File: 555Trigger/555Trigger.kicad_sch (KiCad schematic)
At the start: 23 parts, among them U7 74LVC2G74, U8 74AHC2G00, U9 OPA2333xxD

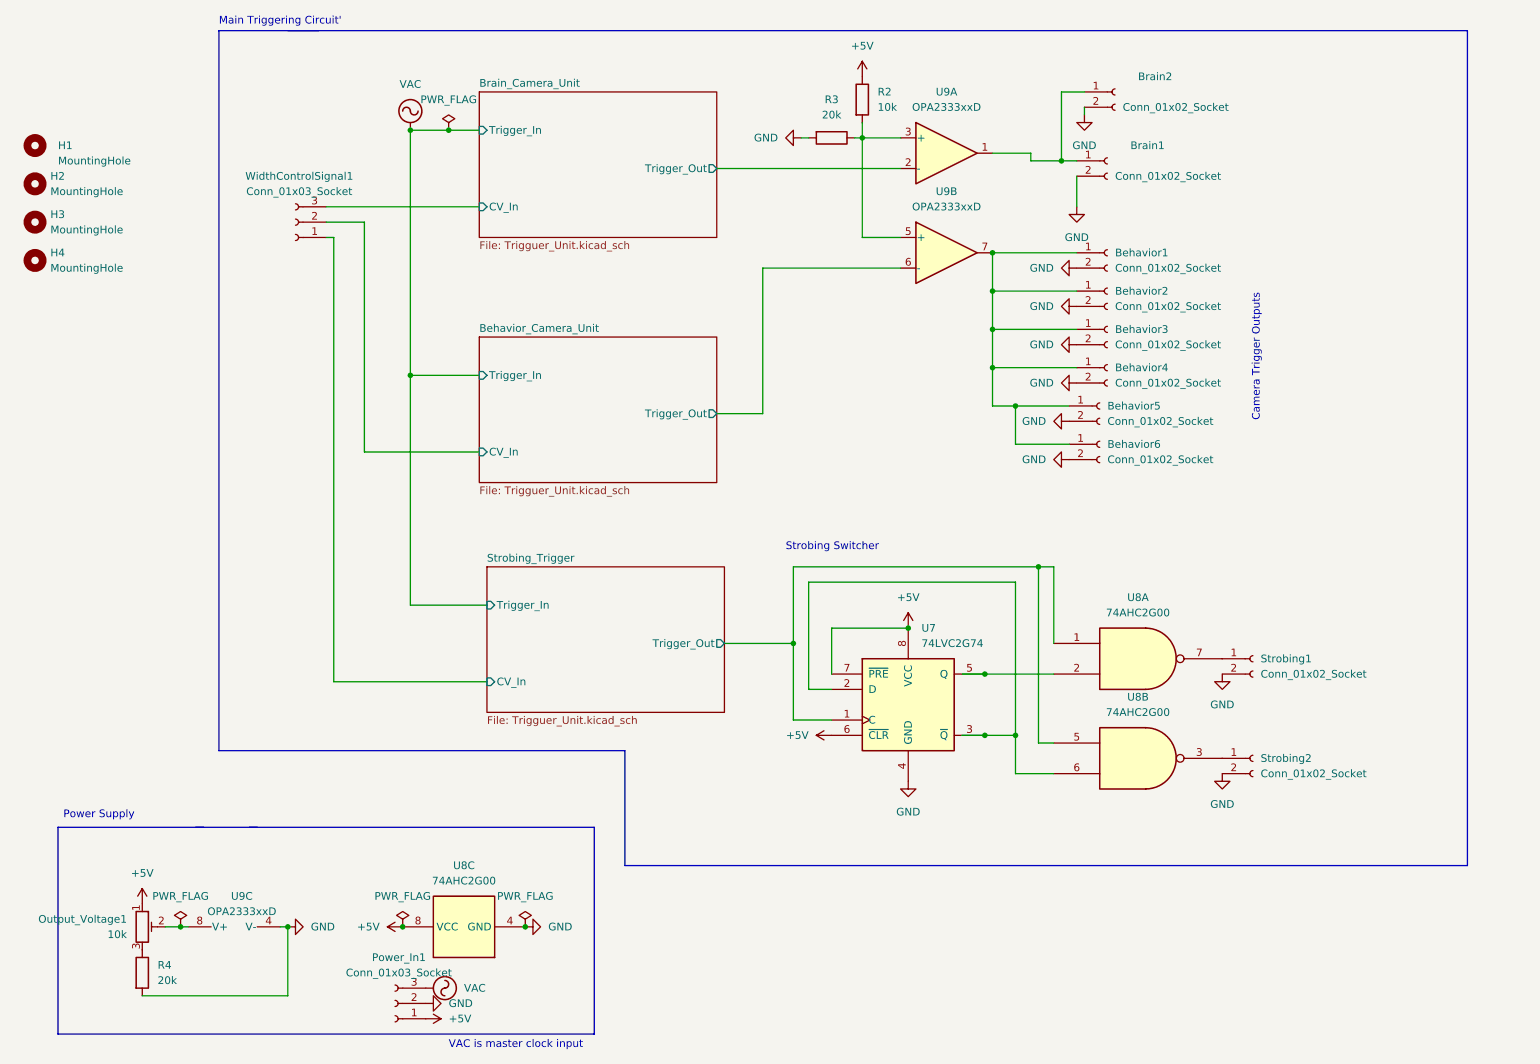
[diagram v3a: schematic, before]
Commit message: changed some components to make manufacturing simpler
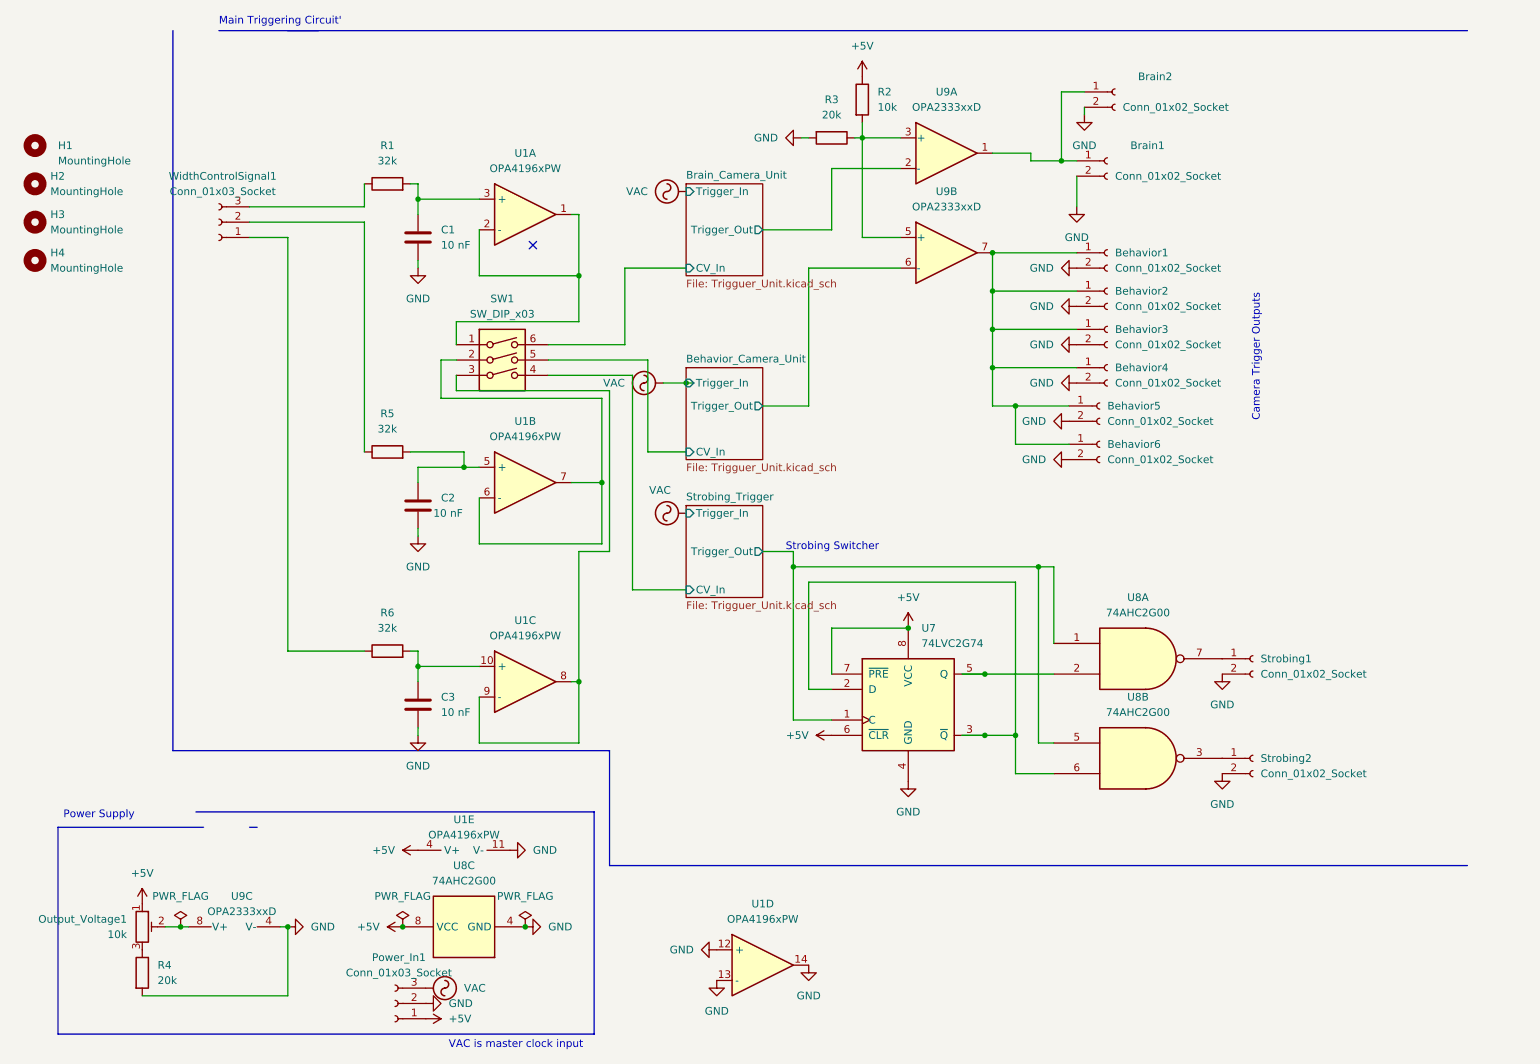
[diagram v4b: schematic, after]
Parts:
- added C1, C2, C3: 10 nF, Capacitor_SMD:C_0603_1608Metric_Pad1.08x0.95mm_HandSolder, symbol Device:C
- added R1, R5, R6: 32k, Resistor_SMD:R_0805_2012Metric_Pad1.20x1.40mm_HandSolder, symbol Device:R
- added SW1: SW_DIP_x03, Button_Switch_SMD:SW_DIP_SPSTx03_Slide_9.78x9.8mm_W8.61mm_P2.54mm, symbol Switch:SW_DIP_x03
- added U1: OPA4196xPW, Package_SO:TSSOP-14_4.4x5mm_P0.65mm, symbol Amplifier_Operational:OPA4196xPW
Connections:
- net +5V: now also U1.4 (V+)
- net Behavior_Camera_Unit/CV_In: now also SW1.5; no longer WidthControlSignal1.2 (Pin_2)
- net Brain_Camera_Unit/CV_In: now also SW1.6; no longer WidthControlSignal1.3 (Pin_3)
- net GND: now also C1.2, C2.2, C3.2, U1.11 (V-), U1.12 (+), U1.13 (-), U1.14
- net Strobing_Trigger/CV_In: now also SW1.4; no longer WidthControlSignal1.1 (Pin_1)
- new net: R6.1, WidthControlSignal1.1 (Pin_1)
- new net: R5.1, WidthControlSignal1.2 (Pin_2)
- new net: R1.1, WidthControlSignal1.3 (Pin_3)
- new net: C1.1, R1.2, U1.3 (+)
- new net: C3.1, R6.2, U1.10 (+)
- new net: C2.1, R5.2, U1.5 (+)
- new net: SW1.3, U1.8, U1.9 (-)
- new net: SW1.1, U1.1, U1.2 (-)
- new net: SW1.2, U1.6 (-), U1.7
- no-connect marks 0 -> 1
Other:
- moved on the sheet: WidthControlSignal1

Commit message: changed components to be easier to order
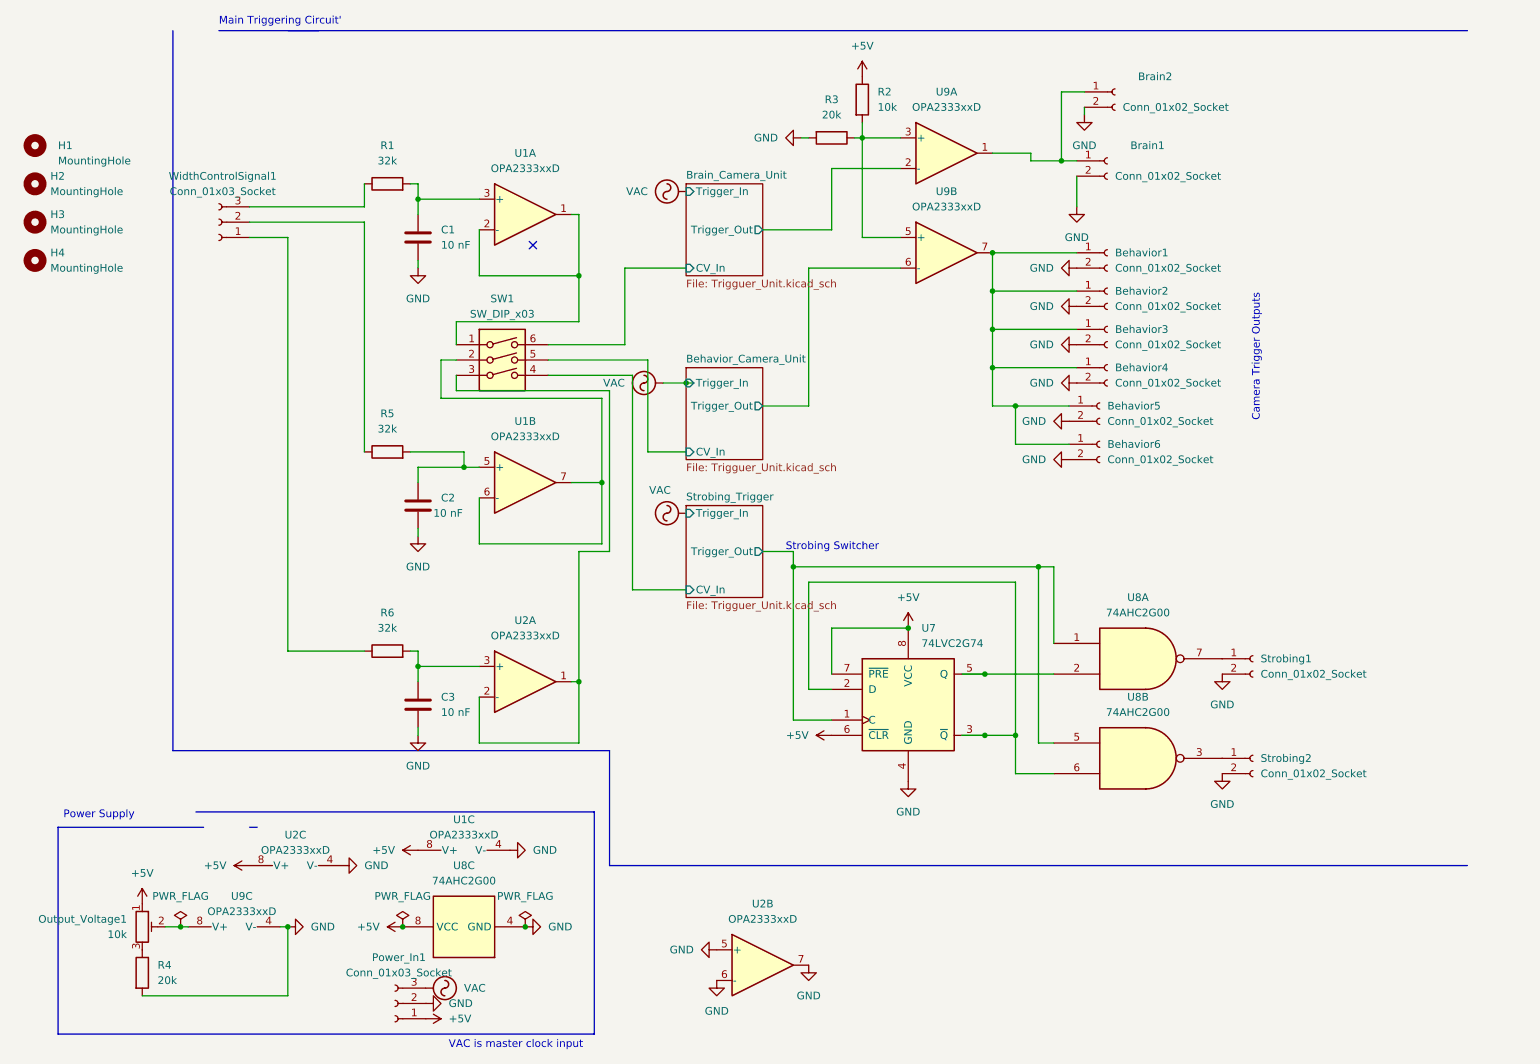
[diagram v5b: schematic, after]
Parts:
- removed U1: OPA4196xPW, Package_SO:TSSOP-14_4.4x5mm_P0.65mm, symbol Amplifier_Operational:OPA4196xPW
- added U1, U2: OPA2333xxD, Package_SO:TSSOP-8_3x3mm_P0.65mm, symbol Amplifier_Operational:OPA2333xxD
- C1, C2, C3: footprint Capacitor_SMD:C_0603_1608Metric_Pad1.08x0.95mm_HandSolder -> Capacitor_SMD:C_0603_1608Metric
- Output_Voltage1: footprint Potentiometer_SMD:Potentiometer_ACP_CA9-VSMD_Vertical -> Potentiometer_SMD:Potentiometer_Bourns_3314J_Vertical
- R1, R2, R3, R4, R5, R6: footprint Resistor_SMD:R_0805_2012Metric_Pad1.20x1.40mm_HandSolder -> Resistor_SMD:R_0402_1005Metric
- U9: footprint Package_DIP:DIP-8_W7.62mm_SMDSocket_SmallPads -> Package_SO:TSSOP-8_3x3mm_P0.65mm
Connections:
- net +5V: now also U1.8 (V+), U2.8 (V+)
- net GND: now also U1.4 (V-), U2.4 (V-), U2.5 (+), U2.6 (-), U2.7
- net at C1.1, R1.2: now also U1.3 (+)
- net at C3.1, R6.2: now also U2.3 (+)
- net at C2.1, R5.2: now also U1.5 (+)
- net at SW1.3: now also U2.1, U2.2 (-)
- net at SW1.1: now also U1.1, U1.2 (-)
- net at SW1.2: now also U1.6 (-), U1.7
